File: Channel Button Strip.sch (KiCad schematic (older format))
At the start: 20 parts, among them SW33 B3F-5050, SW34 B3F-5050, SW35 B3F-5050, SW36 B3F-5050, SW37 B3F-5050, SW38 B3F-5050, SW39 B3F-5050, SW40 B3F-5050

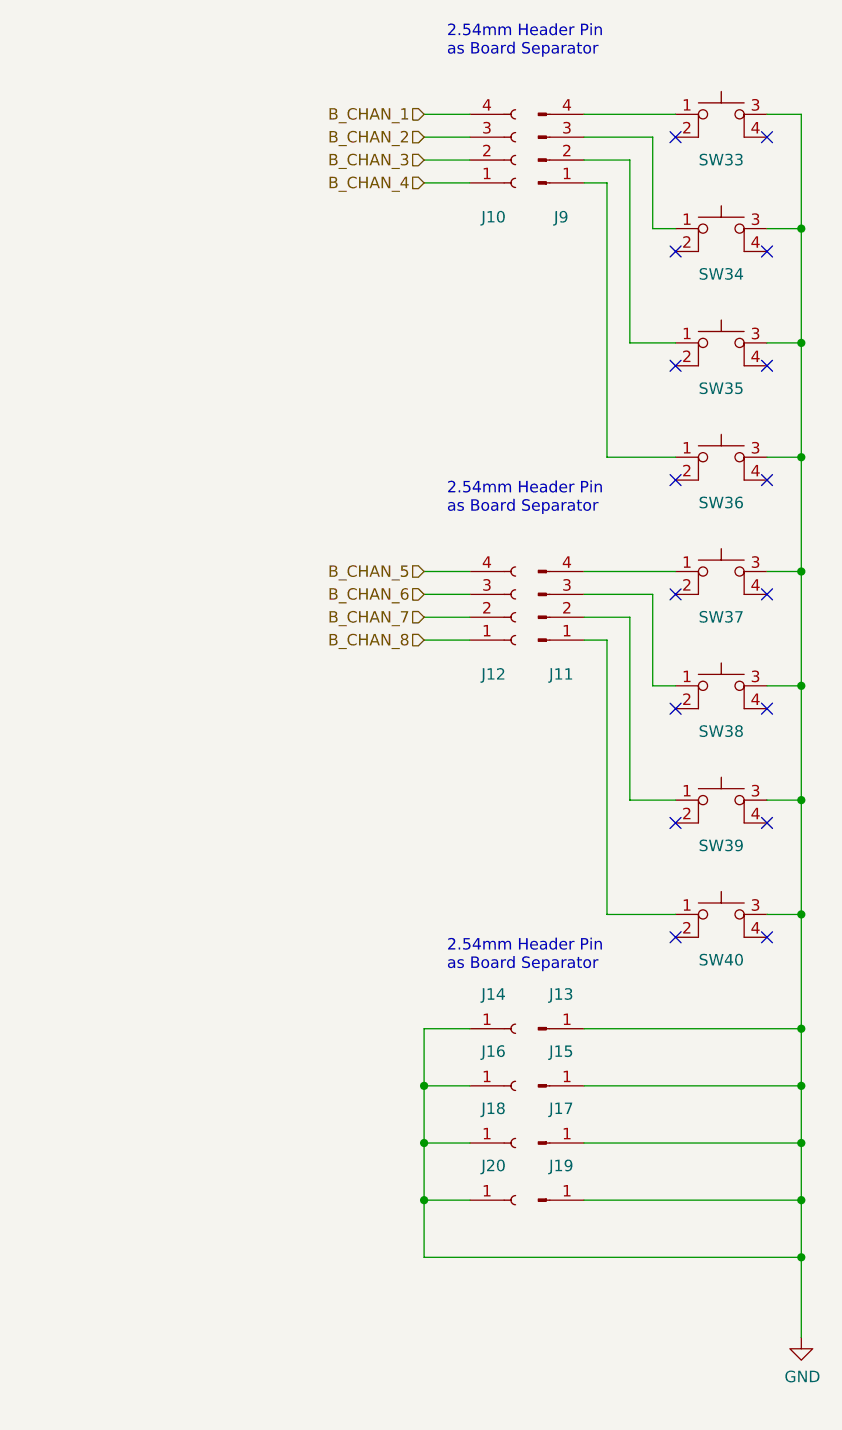
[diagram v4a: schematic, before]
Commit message: Further cleanup and placement
Removed all the connectors to the rails as they're irrelevant to the top boards.

Added all the support headers.

Need to work out the correct routing for the headers but the placement is correct.
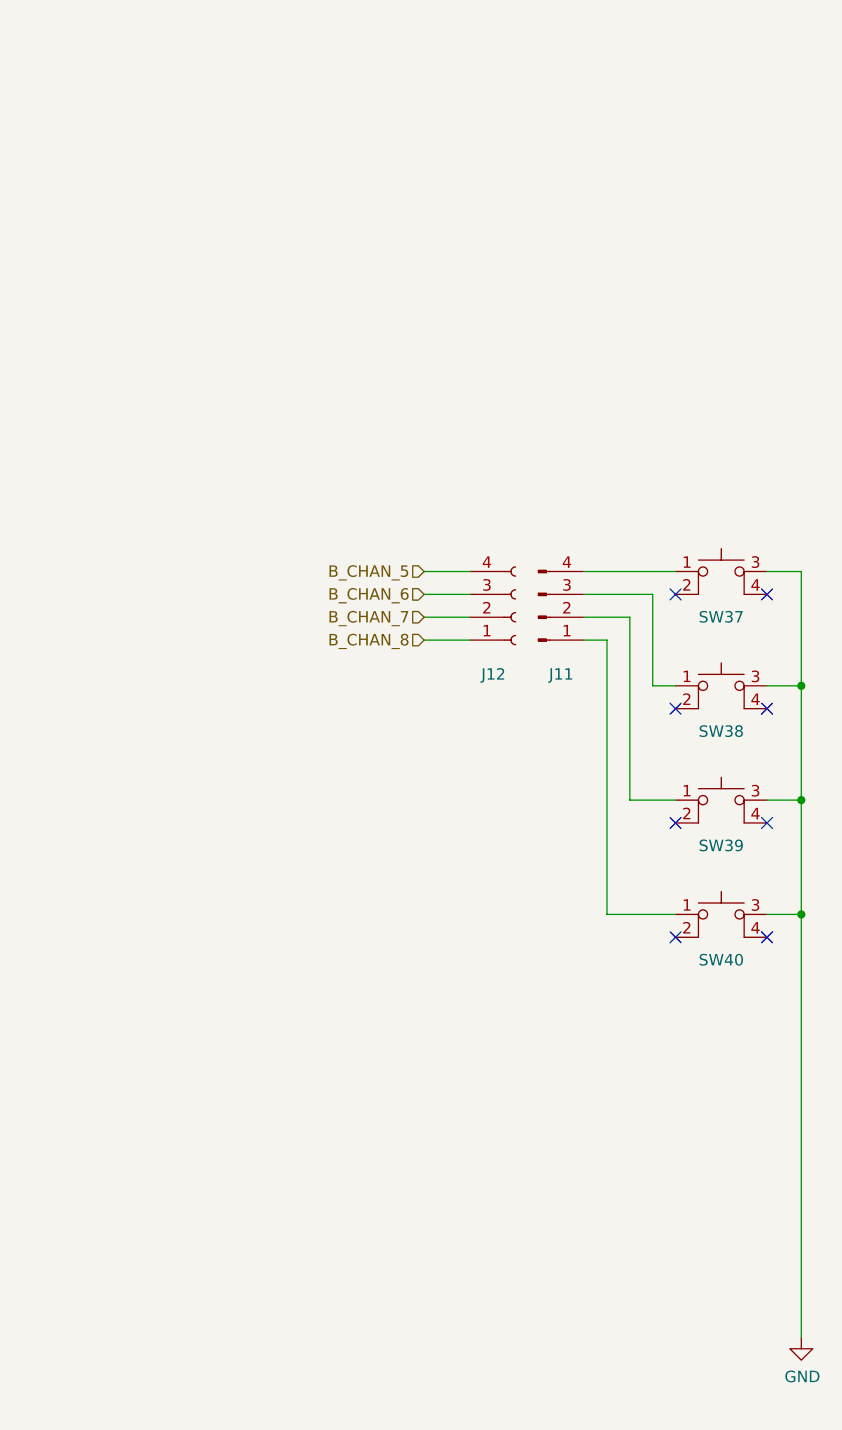
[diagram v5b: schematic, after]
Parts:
- removed J10: ~, Connector_PinSocket_2.54mm:PinSocket_1x04_P2.54mm_Vertical, symbol Connector:Conn_01x04_Female
- removed J13, J15, J17, J19: ~, Connector_PinHeader_2.54mm:PinHeader_1x01_P2.54mm_Vertical, symbol Connector:Conn_01x01_Male
- removed J14, J16, J18, J20: ~, Connector_PinSocket_2.54mm:PinSocket_1x01_P2.54mm_Vertical, symbol Connector:Conn_01x01_Female
- removed J9: ~, Connector_PinHeader_2.54mm:PinHeader_1x04_P2.54mm_Vertical, symbol Connector:Conn_01x04_Male
- removed SW33, SW34, SW35, SW36: B3F-5050, cunabulapress-footprints:Omron_B3F-5050, symbol cp_midi_control_surface_002-rescue:SW_SPST_4_PIN-sw_spst_0
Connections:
- no-connect marks 16 -> 8
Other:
- note removed: "2.54mm Header Pin\nas Board Separator"
